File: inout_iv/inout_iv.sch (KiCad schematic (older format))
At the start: 1 part, among them P1 DIN_41612_128P

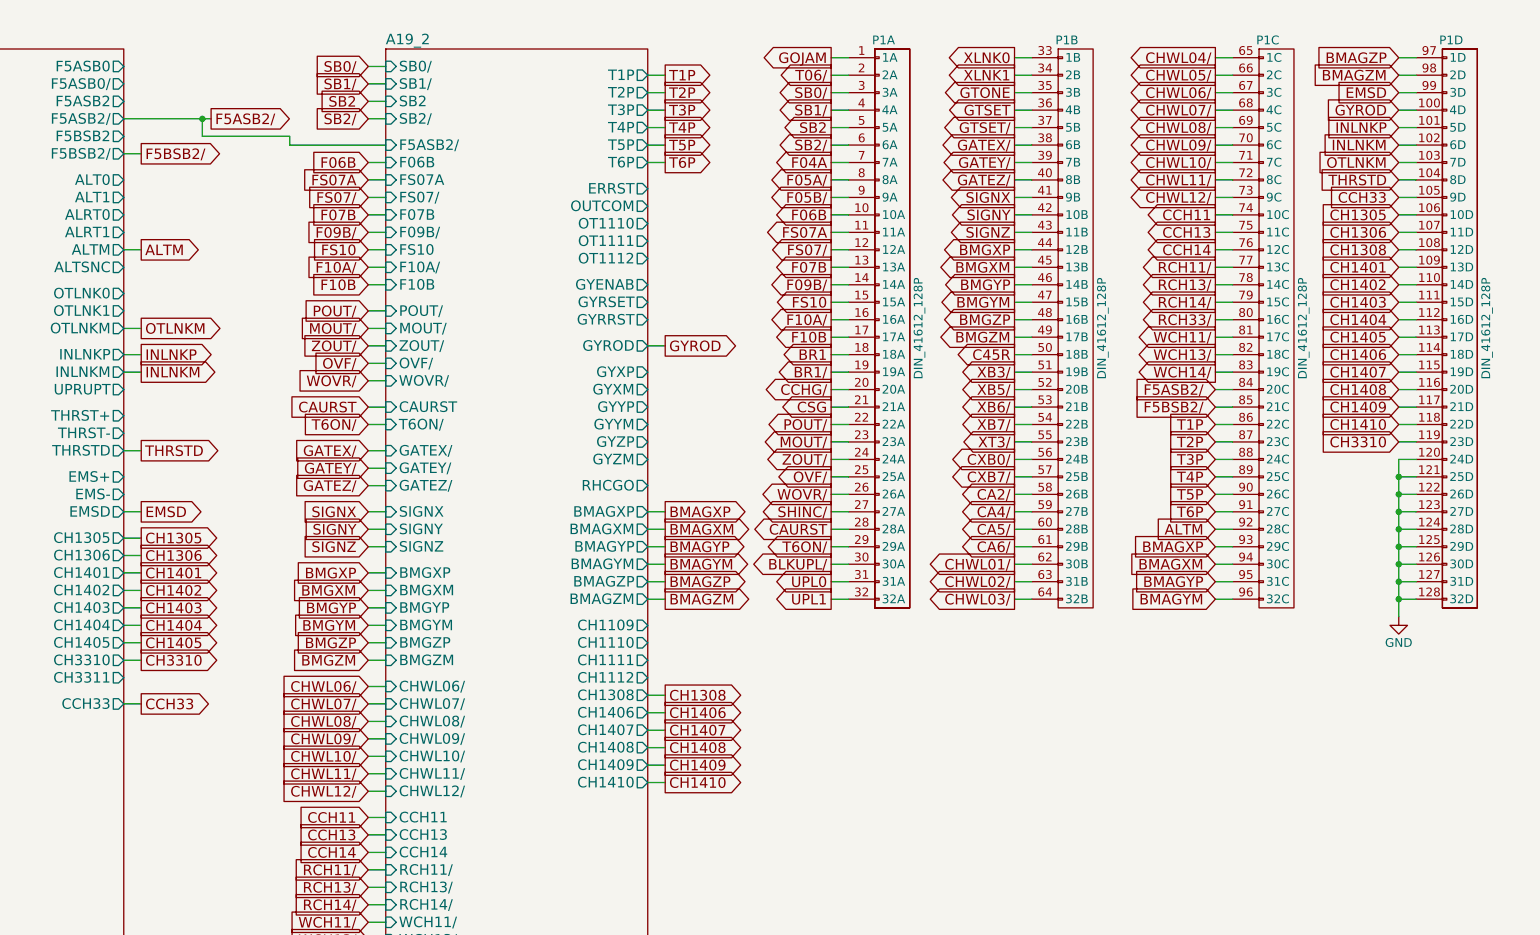
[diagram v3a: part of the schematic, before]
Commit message: Added and tied in Inout VI. Pulled in all PIPA related things. Almost there!
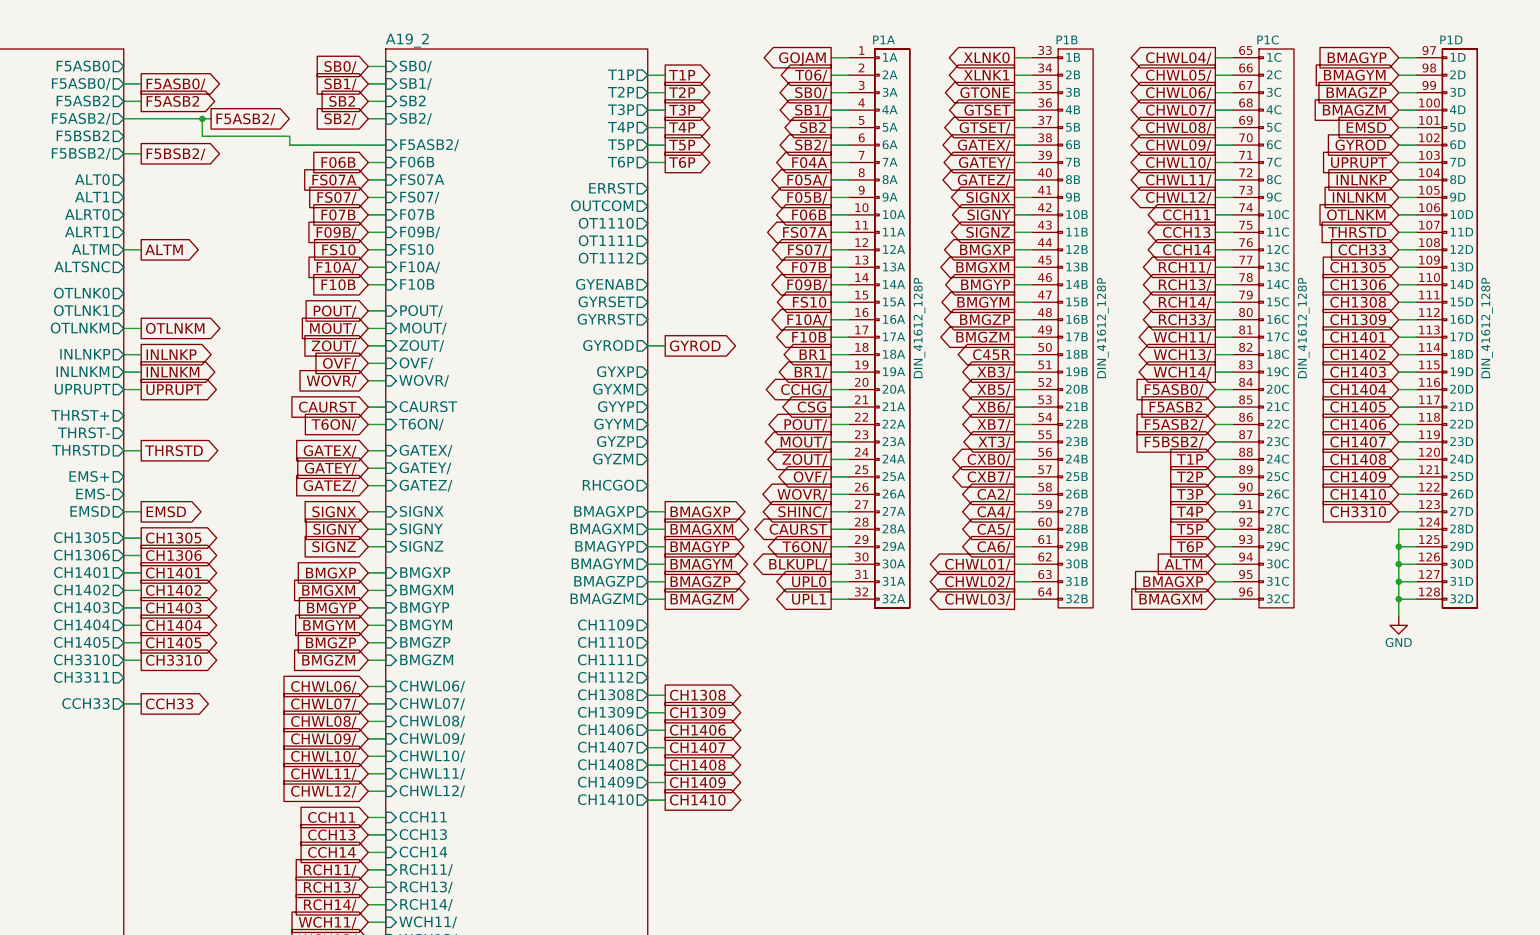
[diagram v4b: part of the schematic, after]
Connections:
- net ALTM: now also P1.94 (30C); no longer P1.92 (28C)
- net BMAGXM: now also P1.96 (32C); no longer P1.94 (30C)
- net BMAGXP: now also P1.95 (31C); no longer P1.93 (29C)
- net BMAGYM: now also P1.98 (2D); no longer P1.96 (32C)
- net BMAGYP: now also P1.97 (1D); no longer P1.95 (31C)
- net BMAGZM: now also P1.100 (4D); no longer P1.98 (2D)
- net BMAGZP: now also P1.99 (3D); no longer P1.97 (1D)
- net CCH33: now also P1.108 (12D); no longer P1.105 (9D)
- net CH1305: now also P1.109 (13D); no longer P1.106 (10D)
- net CH1306: now also P1.110 (14D); no longer P1.107 (11D)
- net CH1308: now also P1.111 (15D); no longer P1.108 (12D)
- net CH1401: now also P1.113 (17D); no longer P1.109 (13D)
- net CH1402: now also P1.114 (18D); no longer P1.110 (14D)
- net CH1403: now also P1.115 (19D); no longer P1.111 (15D)
- net CH1404: now also P1.116 (20D); no longer P1.112 (16D)
- net CH1405: now also P1.117 (21D); no longer P1.113 (17D)
- net CH1406: now also P1.118 (22D); no longer P1.114 (18D)
- net CH1407: now also P1.119 (23D); no longer P1.115 (19D)
- net CH1408: now also P1.120 (24D); no longer P1.116 (20D)
- net CH1409: now also P1.121 (25D); no longer P1.117 (21D)
- net CH1410: now also P1.122 (26D); no longer P1.118 (22D)
- net CH3310: now also P1.123 (27D); no longer P1.119 (23D)
- net EMSD: now also P1.101 (5D); no longer P1.99 (3D)
- net F5ASB2/: now also P1.86 (22C); no longer P1.84 (20C)
- net F5BSB2/: now also P1.87 (23C); no longer P1.85 (21C)
- net GND: no longer P1.120 (24D), P1.121 (25D), P1.122 (26D), P1.123 (27D)
- net GYROD: now also P1.102 (6D); no longer P1.100 (4D)
- net INLNKM: now also P1.105 (9D); no longer P1.102 (6D)
- net INLNKP: now also P1.104 (8D); no longer P1.101 (5D)
- net OTLNKM: now also P1.106 (10D); no longer P1.103 (7D)
- net T1P: now also P1.88 (24C); no longer P1.86 (22C)
- net T2P: now also P1.89 (25C); no longer P1.87 (23C)
- net T3P: now also P1.90 (26C); no longer P1.88 (24C)
- net T4P: now also P1.91 (27C); no longer P1.89 (25C)
- net T5P: now also P1.92 (28C); no longer P1.90 (26C)
- net T6P: now also P1.93 (29C); no longer P1.91 (27C)
- net THRSTD: now also P1.107 (11D); no longer P1.104 (8D)
- new net CH1309: P1.112 (16D)
- new net F5ASB0/: P1.84 (20C)
- new net F5ASB2: P1.85 (21C)
- new net UPRUPT: P1.103 (7D)
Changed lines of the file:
@@
 F20 "WCH14/" I L 4700 6400 60
 F21 "CCH14" I L 4700 5800 60
-F22 "CH1410" O R 6200 5400 60
-F23 "CH1409" O R 6200 5300 60
-F24 "CH1408" O R 6200 5200 60
+F22 "CH1410" O R 6200 5500 60
+F23 "CH1409" O R 6200 5400 60
+F24 "CH1408" O R 6200 5300 60
 F25 "CHWL08/" I L 4700 5050 60
-F26 "CH1407" O R 6200 5100 60
+F26 "CH1407" O R 6200 5200 60
 F27 "CHWL07/" I L 4700 4950 60
-F28 "CH1406" O R 6200 5000 60
+F28 "CH1406" O R 6200 5100 60
 F29 "CHWL06/" I L 4700 4850 60
 F30 "GYROD" O R 6200 2900 60
@@
 F90 "WOVR/" I L 4700 3100 60
 F91 "OVF/" I L 4700 3000 60
+F92 "CH1309" O R 6200 5000 60
 $EndSheet
 Wire Wire Line
@@
 ALTM
 Wire Wire Line
-	9550 3950 9450 3950
-Text GLabel 9450 3950 0    60   Input ~ 0
+	9550 4150 9450 4150
+Text GLabel 9450 4150 0    60   Input ~ 0
 ALTM
 Wire Wire Line
@@
 T6P
 Wire Wire Line
-	9550 3350 9450 3350
-Text GLabel 9450 3350 0    60   Input ~ 0
-T1P
-Wire Wire Line
-	9550 3450 9450 3450
-Text GLabel 9450 3450 0    60   Input ~ 0
-T2P
-Wire Wire Line
 	9550 3550 9450 3550
 Text GLabel 9450 3550 0    60   Input ~ 0
-T3P
+T1P
 Wire Wire Line
 	9550 3650 9450 3650
 Text GLabel 9450 3650 0    60   Input ~ 0
-T4P
+T2P
 Wire Wire Line
 	9550 3750 9450 3750
 Text GLabel 9450 3750 0    60   Input ~ 0
-T5P
+T3P
 Wire Wire Line
 	9550 3850 9450 3850
 Text GLabel 9450 3850 0    60   Input ~ 0
+T4P
+Wire Wire Line
+	9550 3950 9450 3950
+Text GLabel 9450 3950 0    60   Input ~ 0
+T5P
+Wire Wire Line
+	9550 4050 9450 4050
+Text GLabel 9450 4050 0    60   Input ~ 0
 T6P
 Wire Wire Line
@@
 BMAGZM
 Wire Wire Line
-	9550 4050 9450 4050
-Text GLabel 9450 4050 0    60   Input ~ 0
-BMAGXP
-Wire Wire Line
-	9550 4150 9450 4150
-Text GLabel 9450 4150 0    60   Input ~ 0
-BMAGXM
-Wire Wire Line
 	9550 4250 9450 4250
 Text GLabel 9450 4250 0    60   Input ~ 0
-BMAGYP
+BMAGXP
 Wire Wire Line
 	9550 4350 9450 4350
 Text GLabel 9450 4350 0    60   Input ~ 0
-BMAGYM
+BMAGXM
 Wire Wire Line
 	10600 1250 10500 1250
 Text GLabel 10500 1250 0    60   Input ~ 0
-BMAGZP
+BMAGYP
 Wire Wire Line
 	10600 1350 10500 1350
 Text GLabel 10500 1350 0    60   Input ~ 0
+BMAGYM
+Wire Wire Line
+	10600 1450 10500 1450
+Text GLabel 10500 1450 0    60   Input ~ 0
+BMAGZP
+Wire Wire Line
+	10600 1550 10500 1550
+Text GLabel 10500 1550 0    60   Input ~ 0
 BMAGZM
 Wire Wire Line
@@
 CCH33
 Wire Wire Line
-	10600 1450 10500 1450
-Text GLabel 10500 1450 0    60   Input ~ 0
+	10600 1650 10500 1650
+Text GLabel 10500 1650 0    60   Input ~ 0
 EMSD
 Wire Wire Line
@@
 EMSD
 Wire Wire Line
-	10600 2050 10500 2050
-Text GLabel 10500 2050 0    60   Input ~ 0
+	10600 2350 10500 2350
+Text GLabel 10500 2350 0    60   Input ~ 0
 CCH33
 Wire Wire Line
@@
 GYROD
 Wire Wire Line
-	10600 1550 10500 1550
-Text GLabel 10500 1550 0    60   Input ~ 0
+	10600 1750 10500 1750
+Text GLabel 10500 1750 0    60   Input ~ 0
 GYROD
 Wire Wire Line
@@
 INLNKP
 Wire Wire Line
-	10600 1650 10500 1650
-Text GLabel 10500 1650 0    60   Input ~ 0
+	10600 1950 10500 1950
+Text GLabel 10500 1950 0    60   Input ~ 0
 INLNKP
 Wire Wire Line
-	10600 1750 10500 1750
-Text GLabel 10500 1750 0    60   Input ~ 0
+	10600 2050 10500 2050
+Text GLabel 10500 2050 0    60   Input ~ 0
 INLNKM
 Wire Wire Line
@@
 OTLNKM
 Wire Wire Line
-	10600 1850 10500 1850
-Text GLabel 10500 1850 0    60   Input ~ 0
+	10600 2150 10500 2150
+Text GLabel 10500 2150 0    60   Input ~ 0
 OTLNKM
 Wire Wire Line
@@
 THRSTD
 Wire Wire Line
-	10600 1950 10500 1950
-Text GLabel 10500 1950 0    60   Input ~ 0
+	10600 2250 10500 2250
+Text GLabel 10500 2250 0    60   Input ~ 0
 THRSTD
 Wire Wire Line
@@
 CH1308
 Wire Wire Line
-	6200 5000 6300 5000
-Text GLabel 6300 5000 2    60   Output ~ 0
-CH1406
-Wire Wire Line
 	6200 5100 6300 5100
 Text GLabel 6300 5100 2    60   Output ~ 0
-CH1407
+CH1406
 Wire Wire Line
 	6200 5200 6300 5200
 Text GLabel 6300 5200 2    60   Output ~ 0
-CH1408
+CH1407
 Wire Wire Line
 	6200 5300 6300 5300
 Text GLabel 6300 5300 2    60   Output ~ 0
-CH1409
+CH1408
 Wire Wire Line
 	6200 5400 6300 5400
 Text GLabel 6300 5400 2    60   Output ~ 0
+CH1409
+Wire Wire Line
+	6200 5500 6300 5500
+Text GLabel 6300 5500 2    60   Output ~ 0
 CH1410
-Wire Wire Line
-	10600 2150 10500 2150
-Text GLabel 10500 2150 0    60   Input ~ 0
-CH1305
-Wire Wire Line
-	10600 2250 10500 2250
-Text GLabel 10500 2250 0    60   Input ~ 0
-CH1306
 Wire Wire Line
 	10600 2450 10500 2450
 Text GLabel 10500 2450 0    60   Input ~ 0
-CH1401
+CH1305
 Wire Wire Line
 	10600 2550 10500 2550
 Text GLabel 10500 2550 0    60   Input ~ 0
+CH1306
+Wire Wire Line
+	10600 2850 10500 2850
+Text GLabel 10500 2850 0    60   Input ~ 0
+CH1401
+Wire Wire Line
+	10600 2950 10500 2950
+Text GLabel 10500 2950 0    60   Input ~ 0
 CH1402
+Wire Wire Line
+	10600 3050 10500 3050
+Text GLabel 10500 3050 0    60   Input ~ 0
+CH1403
+Wire Wire Line
+	10600 3150 10500 3150
+Text GLabel 10500 3150 0    60   Input ~ 0
+CH1404
+Wire Wire Line
+	10600 3250 10500 3250
+Text GLabel 10500 3250 0    60   Input ~ 0
+CH1405
+Wire Wire Line
+	10600 3850 10500 3850
+Text GLabel 10500 3850 0    60   Input ~ 0
+CH3310
 Wire Wire Line
 	10600 2650 10500 2650
 Text GLabel 10500 2650 0    60   Input ~ 0
-CH1403
-Wire Wire Line
-	10600 2750 10500 2750
-Text GLabel 10500 2750 0    60   Input ~ 0
-CH1404
-Wire Wire Line
-	10600 2850 10500 2850
-Text GLabel 10500 2850 0    60   Input ~ 0
-CH1405
+CH1308
+Wire Wire Line
+	10600 3350 10500 3350
+Text GLabel 10500 3350 0    60   Input ~ 0
+CH1406
 Wire Wire Line
 	10600 3450 10500 3450
 Text GLabel 10500 3450 0    60   Input ~ 0
-CH3310
-Wire Wire Line
-	10600 2350 10500 2350
-Text GLabel 10500 2350 0    60   Input ~ 0
-CH1308
-Wire Wire Line
-	10600 2950 10500 2950
-Text GLabel 10500 2950 0    60   Input ~ 0
-CH1406
-Wire Wire Line
-	10600 3050 10500 3050
-Text GLabel 10500 3050 0    60   Input ~ 0
 CH1407
 Wire Wire Line
-	10600 3150 10500 3150
-Text GLabel 10500 3150 0    60   Input ~ 0
+	10600 3550 10500 3550
+Text GLabel 10500 3550 0    60   Input ~ 0
 CH1408
 Wire Wire Line
-	10600 3250 10500 3250
-Text GLabel 10500 3250 0    60   Input ~ 0
+	10600 3650 10500 3650
+Text GLabel 10500 3650 0    60   Input ~ 0
 CH1409
 Wire Wire Line
-	10600 3350 10500 3350
-Text GLabel 10500 3350 0    60   Input ~ 0
+	10600 3750 10500 3750
+Text GLabel 10500 3750 0    60   Input ~ 0
 CH1410
 Wire Wire Line
-	10500 3650 10600 3650
-Connection ~ 10500 3650
-Wire Wire Line
-	10500 3750 10600 3750
-Connection ~ 10500 3750
-Wire Wire Line
-	10500 3850 10600 3850
-Connection ~ 10500 3850
-Wire Wire Line
 	10500 3950 10600 3950
-Connection ~ 10500 3950
-Wire Wire Line
-	10500 3550 10600 3550
 Text GLabel 3700 1600 2    60   Output ~ 0
 F5ASB2/
@@
 	4150 1750 4700 1750
 Wire Wire Line
-	10500 3550 10500 4450
+	9550 3350 9450 3350
+Text GLabel 9450 3350 0    60   Input ~ 0
+F5ASB2/
+Wire Wire Line
+	9550 3450 9450 3450
+Text GLabel 9450 3450 0    60   Input ~ 0
+F5BSB2/
+Wire Wire Line
+	3200 1500 3300 1500
+Text GLabel 3300 1500 2    60   Output ~ 0
+F5ASB2
+Wire Wire Line
+	3200 1400 3300 1400
+Text GLabel 3300 1400 2    60   Output ~ 0
+F5ASB0/
+Wire Wire Line
+	9550 3250 9450 3250
+Text GLabel 9450 3250 0    60   Input ~ 0
+F5ASB2
 Wire Wire Line
 	9550 3150 9450 3150
 Text GLabel 9450 3150 0    60   Input ~ 0
-F5ASB2/
-Wire Wire Line
-	9550 3250 9450 3250
-Text GLabel 9450 3250 0    60   Input ~ 0
-F5BSB2/
+F5ASB0/
+Wire Wire Line
+	6200 5000 6300 5000
+Text GLabel 6300 5000 2    60   Output ~ 0
+CH1309
+Wire Wire Line
+	10600 2750 10500 2750
+Text GLabel 10500 2750 0    60   Input ~ 0
+CH1309
+Wire Wire Line
+	3200 3150 3300 3150
+Text GLabel 3300 3150 2    60   Output ~ 0
+UPRUPT
+Wire Wire Line
+	10500 3950 10500 4450
+Wire Wire Line
+	10600 1850 10500 1850
+Text GLabel 10500 1850 0    60   Input ~ 0
+UPRUPT
 $EndSCHEMATC

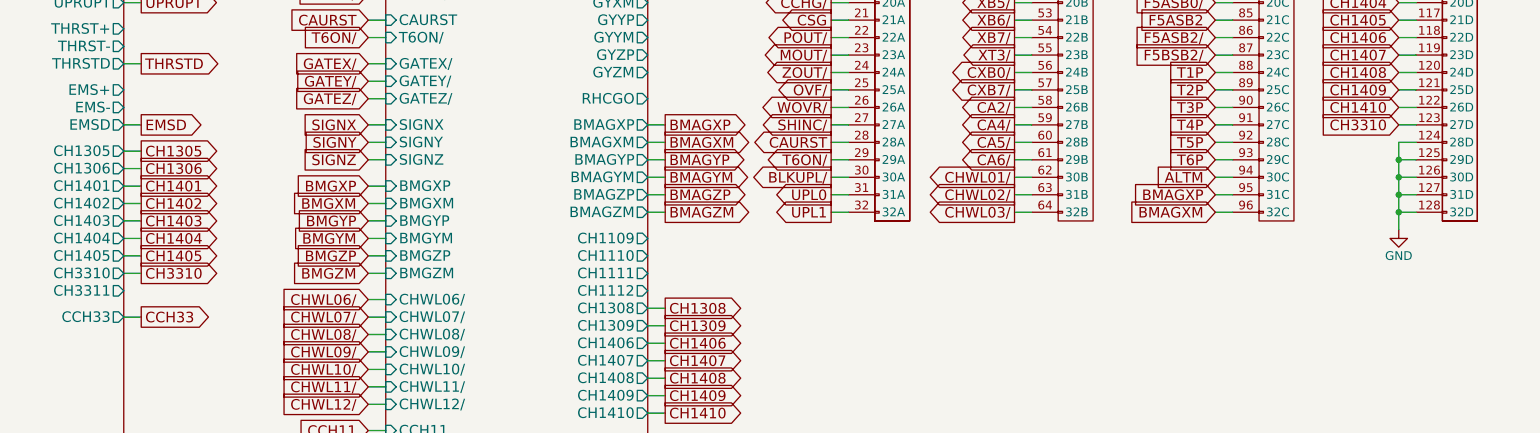
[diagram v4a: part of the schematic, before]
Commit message: Added and tied in Inout VII, the final logic module!
I still need to comb through the schematics to see if there are any
stray gates I missed. The initial conditions are also pretty much
guaranteed to be wrong. But it's mostly all there!
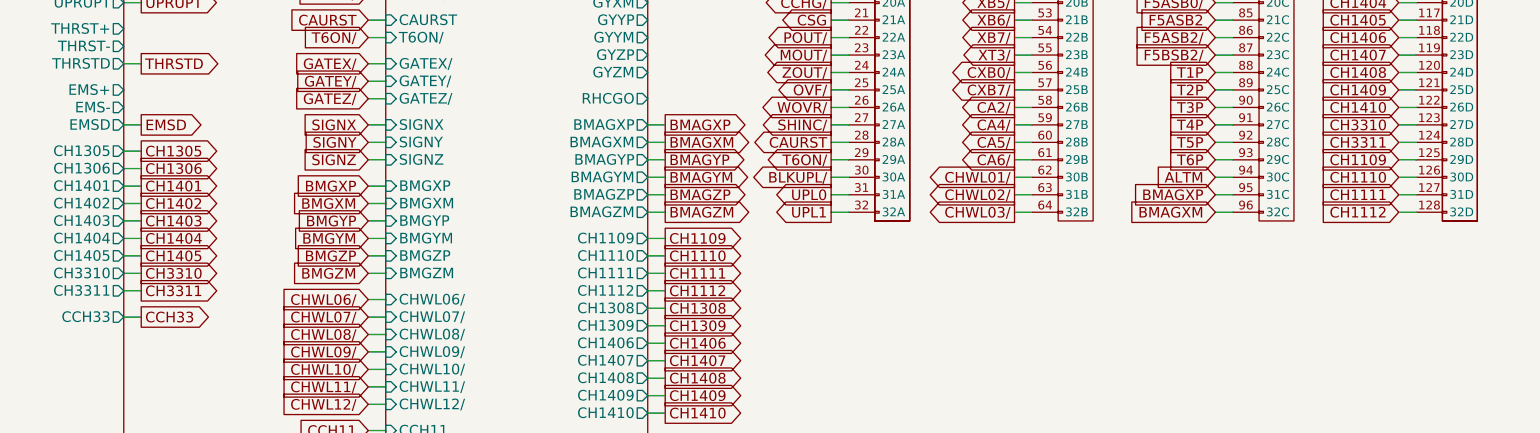
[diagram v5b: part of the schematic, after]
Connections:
- net GND: no longer P1.124 (28D), P1.125 (29D), P1.126 (30D), P1.127 (31D), P1.128 (32D)
- new net CH1109: P1.125 (29D)
- new net CH1110: P1.126 (30D)
- new net CH1111: P1.127 (31D)
- new net CH1112: P1.128 (32D)
- new net CH3311: P1.124 (28D)
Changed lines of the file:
@@
-	1    0    0    -1
-$EndComp
-Wire Wire Line
-	10500 4050 10600 4050
-Connection ~ 10500 4050
-Wire Wire Line
-	10500 4150 10600 4150
-Connection ~ 10500 4150
-Wire Wire Line
-	10500 4250 10600 4250
-Connection ~ 10500 4250
-Wire Wire Line
-	10500 4350 10600 4350
-Connection ~ 10500 4350
-$Comp
-L GND #PWR01
-U 1 1 57F2F9C5
-P 10500 4450
-F 0 "#PWR01" H 10500 4200 50  0001 C CNN
-F 1 "GND" H 10500 4300 50  0000 C CNN
-F 2 "" H 10500 4450 60  0000 C CNN
-F 3 "" H 10500 4450 60  0000 C CNN
-	1    10500 4450
 	1    0    0    -1
 $EndComp
@@
 Text GLabel 10500 3750 0    60   Input ~ 0
 CH1410
-Wire Wire Line
-	10500 3950 10600 3950
 Text GLabel 3700 1600 2    60   Output ~ 0
 F5ASB2/
@@
 UPRUPT
 Wire Wire Line
-	10500 3950 10500 4450
-Wire Wire Line
 	10600 1850 10500 1850
 Text GLabel 10500 1850 0    60   Input ~ 0
 UPRUPT
+Wire Wire Line
+	3200 4800 3300 4800
+Text GLabel 3300 4800 2    60   Output ~ 0
+CH3311
+Wire Wire Line
+	10600 3950 10500 3950
+Text GLabel 10500 3950 0    60   Input ~ 0
+CH3311
+Wire Wire Line
+	6200 4500 6300 4500
+Text GLabel 6300 4500 2    60   Output ~ 0
+CH1109
+Wire Wire Line
+	6200 4600 6300 4600
+Text GLabel 6300 4600 2    60   Output ~ 0
+CH1110
+Wire Wire Line
+	6200 4700 6300 4700
+Text GLabel 6300 4700 2    60   Output ~ 0
+CH1111
+Wire Wire Line
+	6200 4800 6300 4800
+Text GLabel 6300 4800 2    60   Output ~ 0
+CH1112
+Wire Wire Line
+	10600 4050 10500 4050
+Text GLabel 10500 4050 0    60   Input ~ 0
+CH1109
+Wire Wire Line
+	10600 4150 10500 4150
+Text GLabel 10500 4150 0    60   Input ~ 0
+CH1110
+Wire Wire Line
+	10600 4250 10500 4250
+Text GLabel 10500 4250 0    60   Input ~ 0
+CH1111
+Wire Wire Line
+	10600 4350 10500 4350
+Text GLabel 10500 4350 0    60   Input ~ 0
+CH1112
 $EndSCHEMATC
